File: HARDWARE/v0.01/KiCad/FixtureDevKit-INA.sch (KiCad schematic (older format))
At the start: 40 parts, among them J100 INA_43, J101 INA_43, J102 INA_41, J103 INA_43, J92 INA_40, J93 INA_40, J94 INA_42, J95 INA_42, J96 INA_40, J97 INA_42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

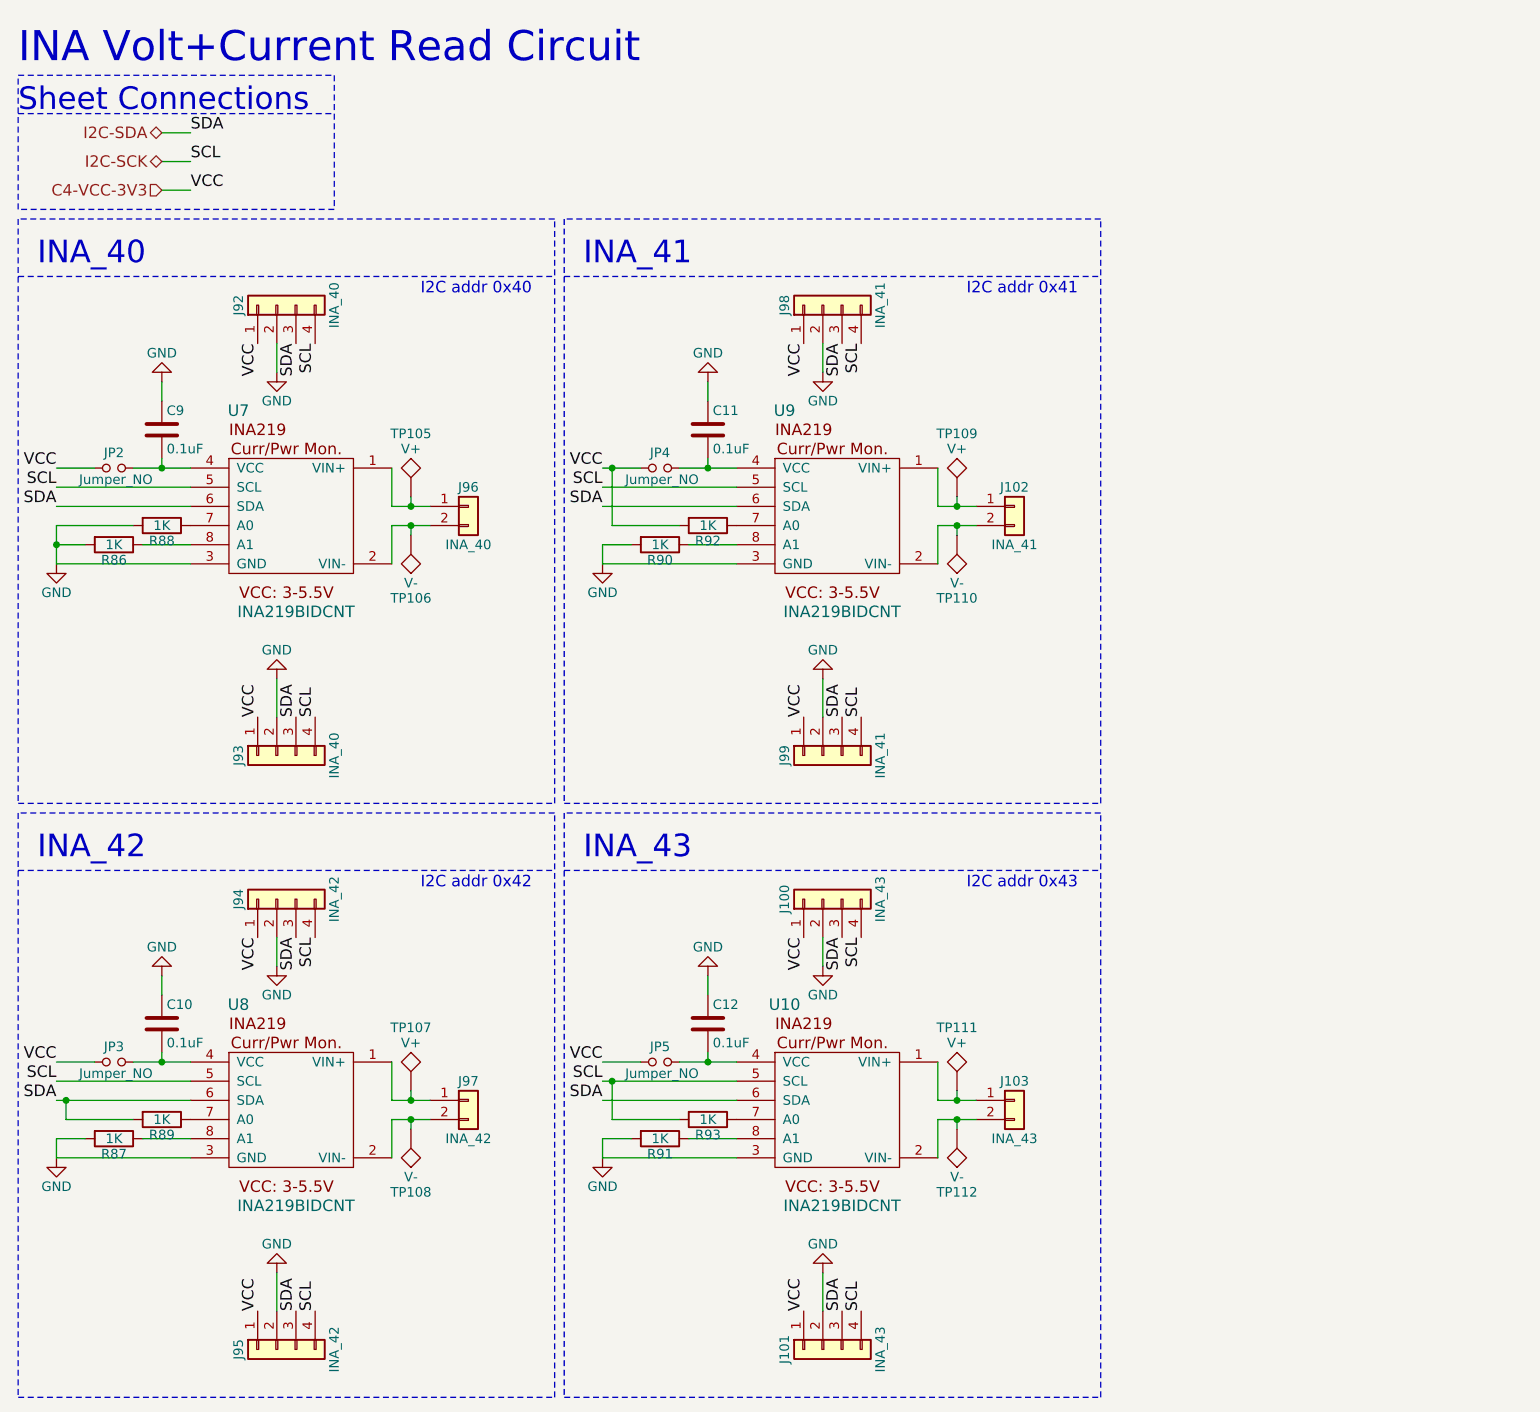
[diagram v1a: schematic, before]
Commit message: quasi-redoing entire schematic and layout
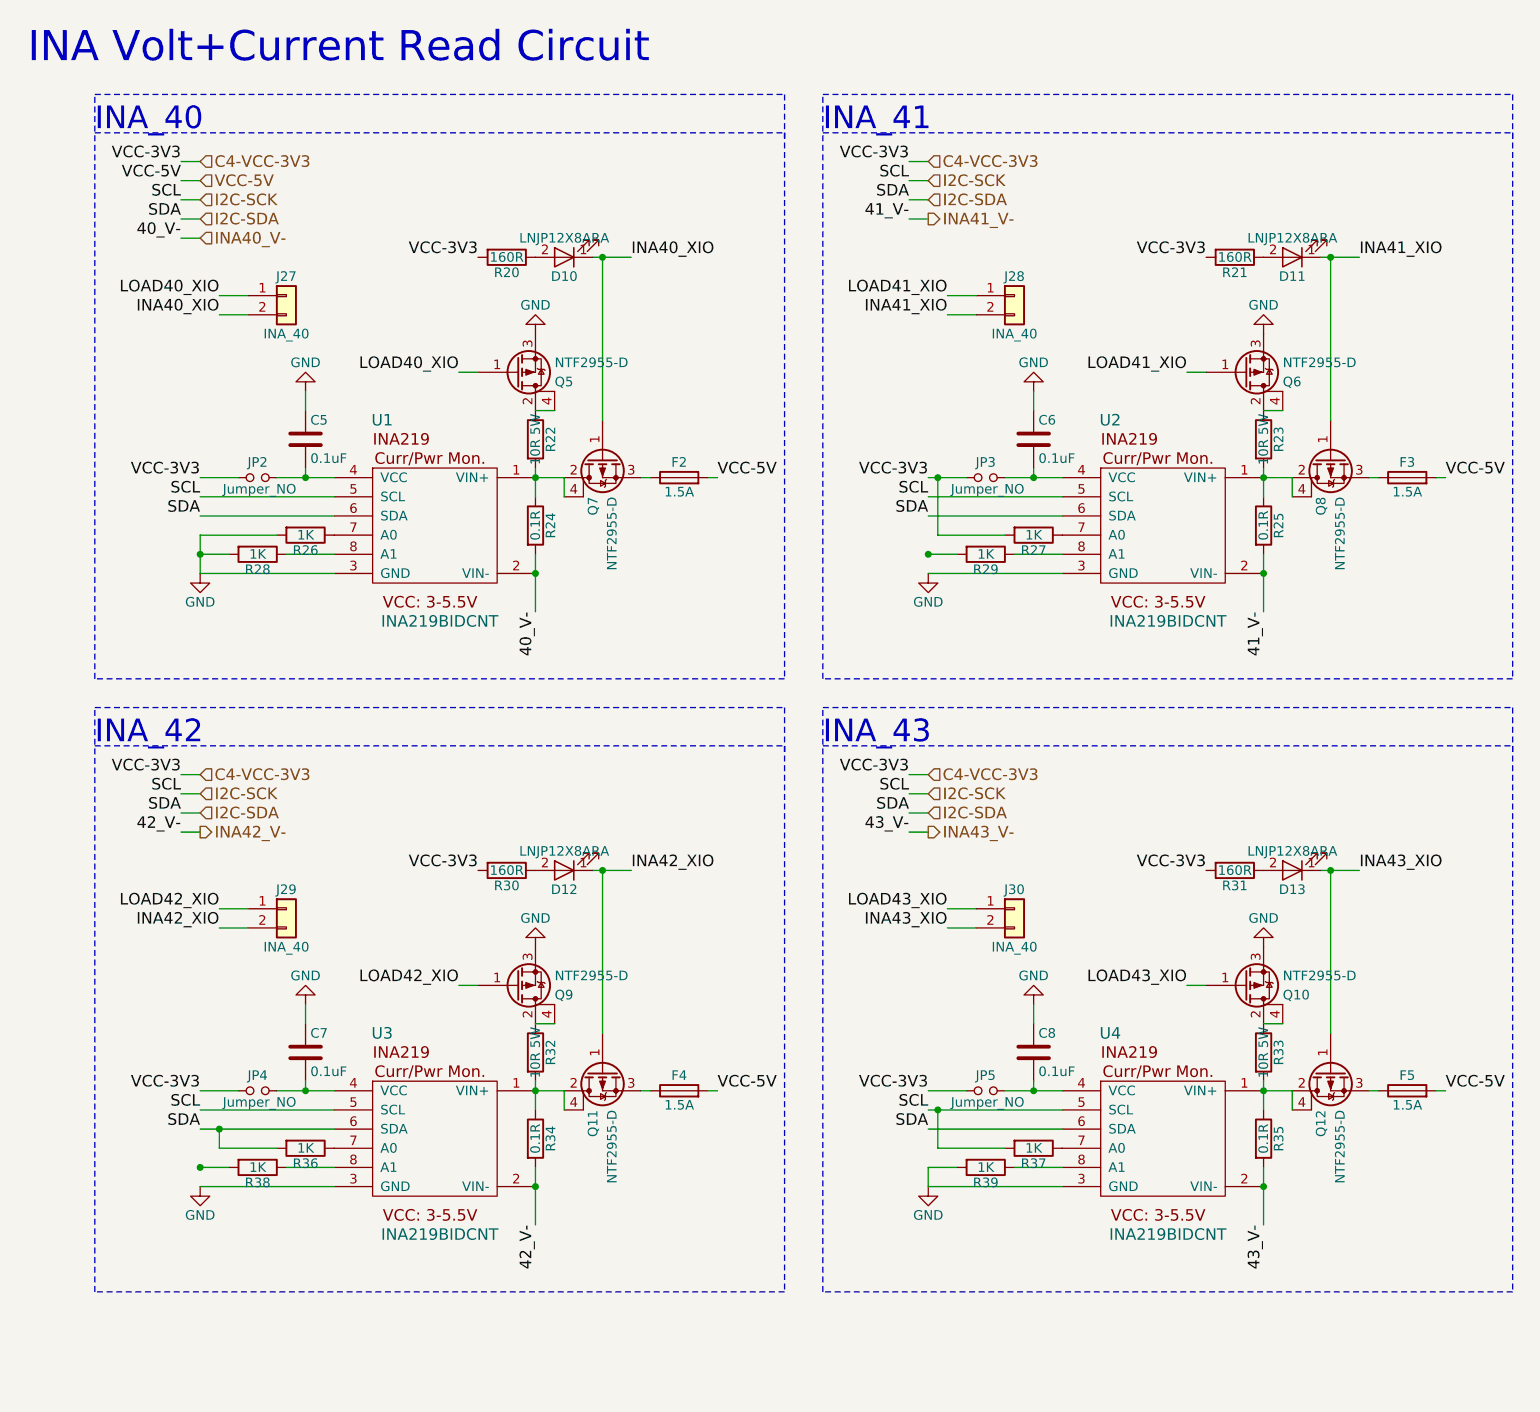
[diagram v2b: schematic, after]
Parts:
- removed C10, C11, C12: 0.1uF, Capacitors_SMD:C_0805_HandSoldering, symbol C
- removed J100, J101: INA_43, Pin_Headers:Pin_Header_Straight_1x04_Pitch2.54mm, symbol Conn_01x04
- removed J102: INA_41, Pin_Headers:Pin_Header_Straight_1x02_Pitch2.54mm, symbol Conn_01x02
- removed J103: INA_43, Pin_Headers:Pin_Header_Straight_1x02_Pitch2.54mm, symbol Conn_01x02
- removed J92, J93: INA_40, Pin_Headers:Pin_Header_Straight_1x04_Pitch2.54mm, symbol Conn_01x04
- removed J94, J95: INA_42, Pin_Headers:Pin_Header_Straight_1x04_Pitch2.54mm, symbol Conn_01x04
- removed J96: INA_40, Pin_Headers:Pin_Header_Straight_1x02_Pitch2.54mm, symbol Conn_01x02
- removed J97: INA_42, Pin_Headers:Pin_Header_Straight_1x02_Pitch2.54mm, symbol Conn_01x02
- removed J98, J99: INA_41, Pin_Headers:Pin_Header_Straight_1x04_Pitch2.54mm, symbol Conn_01x04
- removed R87, R89, R90, R91, R92, R93: 1K, Resistors_SMD:R_0805_HandSoldering, symbol R
- removed TP105, TP107, TP109, TP111: V+, TestPoint:TestPoint, symbol TEST
- removed TP106, TP108, TP110, TP112: V-, TestPoint:TestPoint, symbol TEST
- removed U10, U8, U9: INA219BIDCNT, INA219BIDCNR:SOT65P280X145-8N, symbol INA219BIDCNT
- added C6, C7, C8: 0.1uF, Capacitors_SMD:C_0805_HandSoldering, symbol C
- added D10, D11, D12, D13: LNJP12X8ARA, 1206:1206, symbol LED
- added F2, F3, F4, F5: 1.5A, 1206:1206, symbol Fuse
- added J27, J28, J29, J30: INA_40, Pin_Headers:Pin_Header_Straight_1x02_Pitch2.54mm, symbol Conn_01x02
- added Q10, Q11, Q12, Q5, Q6, Q7, Q8, Q9: NTF2955-D, NTF2955T1G:SOT230P700X180-4N, symbol Q_PMOS_GDSD
- added R20, R21, R30, R31: 160R, Resistors_SMD:R_0805_HandSoldering, symbol R
- added R22, R23, R32, R33: 10R 5W, RES_TWM3J560E:RES_TWM3J560E, symbol R
- added R24, R25, R34, R35: 0.1R, Resistors_SMD:R_0805_HandSoldering, symbol R
- added R27, R29, R36, R37, R38, R39: 1K, Resistors_SMD:R_0805_HandSoldering, symbol R
- added U2, U3, U4: INA219BIDCNT, INA219BIDCNR:SOT65P280X145-8N, symbol INA219BIDCNT
- renumbered C9 to C5, R88 to R26, R86 to R28, U7 to U1
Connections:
- net C4-VCC-3V3: now also R20.2, R21.2, R27.2, R30.2, R31.2
- net GND: now also C6.1, C7.1, C8.1, Q10.3 (S), Q5.3 (S), Q6.3 (S), Q9.3 (S), R39.2, U2.3 (GND), U3.3 (GND), U4.3 (GND)
- net I2C-SCK: now also R37.2, U2.5 (SCL), U3.5 (SCL), U4.5 (SCL)
- net I2C-SDA: now also R36.2, U2.6 (SDA), U3.6 (SDA), U4.6 (SDA)
- net at U1.1 (VIN+): now also Q7.2 (D), Q7.4 (D), R22.2, R24.1
- net INA40_V-: now reaches U1.2 (VIN-)
- net INA40_V-: now also R24.2
- net at JP4.2: now also C7.2, U3.4 (VCC)
- net at JP3.2: now also C6.2, U2.4 (VCC)
- net at JP5.2: now also C8.2, U4.4 (VCC)
- new net: F2.1, Q7.3 (S)
- new net: D10.2 (A), R20.1
- new net: Q5.2 (D), Q5.4 (D), R22.1
- new net: R27.1, U2.7 (A0)
- new net: R29.1, U2.8 (A1)
- new net: Q8.2 (D), Q8.4 (D), R23.2, R25.1, U2.1 (VIN+)
- new net: F3.1, Q8.3 (S)
- new net: D11.2 (A), R21.1
- new net: Q6.2 (D), Q6.4 (D), R23.1
- new net: R36.1, U3.7 (A0)
- new net: R38.1, U3.8 (A1)
- new net: Q11.2 (D), Q11.4 (D), R32.2, R34.1, U3.1 (VIN+)
- new net: F4.1, Q11.3 (S)
- new net: D12.2 (A), R30.1
- new net: Q9.2 (D), Q9.4 (D), R32.1
- new net: R37.1, U4.7 (A0)
- new net: R39.1, U4.8 (A1)
- new net: Q12.2 (D), Q12.4 (D), R33.2, R35.1, U4.1 (VIN+)
- new net: F5.1, Q12.3 (S)
- new net: D13.2 (A), R31.1
- new net: Q10.2 (D), Q10.4 (D), R33.1
- new net INA40_XIO: D10.1 (K), J27.2 (Pin_2), Q7.1 (G)
- new net INA41_V-: R25.2, U2.2 (VIN-)
- new net INA41_XIO: D11.1 (K), J28.2 (Pin_2), Q8.1 (G)
- new net INA42_V-: R34.2, U3.2 (VIN-)
- new net INA42_XIO: D12.1 (K), J29.2 (Pin_2), Q11.1 (G)
- new net INA43_V-: R35.2, U4.2 (VIN-)
- new net INA43_XIO: D13.1 (K), J30.2 (Pin_2), Q12.1 (G)
- new net LOAD40_XIO: J27.1 (Pin_1), Q5.1 (G)
- new net LOAD41_XIO: J28.1 (Pin_1), Q6.1 (G)
- new net LOAD42_XIO: J29.1 (Pin_1), Q9.1 (G)
- new net LOAD43_XIO: J30.1 (Pin_1), Q10.1 (G)
- new net VCC-5V: F2.2, F3.2, F4.2, F5.2
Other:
- note added: "INA_41"
- note removed: "I2C addr 0x40"
- note removed: "I2C addr 0x41\n"
- note removed: "I2C addr 0x42"
- note removed: "I2C addr 0x43"
- note removed: "INA_41\n"
- note removed: "Sheet Connections"
- moved on the sheet: C5, JP2, R26, R28, U1

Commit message: updating rough layout
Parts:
- added D18, D19, D20, D21: LNJP12X8ARA, 1206:1206, symbol LED
- added R17, R18, R56, R57: 160R, Resistors_SMD:R_0805_HandSoldering, symbol R
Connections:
- net C4-VCC-3V3: now also R17.2, R18.2, R56.2, R57.2
- net GND: now also R29.2, R38.2
- net LOAD40_XIO: now also D18.1 (K)
- net LOAD41_XIO: now also D19.1 (K)
- net LOAD42_XIO: now also D20.1 (K)
- net LOAD43_XIO: now also D21.1 (K)
- new net: D18.2 (A), R17.1
- new net: D19.2 (A), R18.1
- new net: D21.2 (A), R57.1
- new net: D20.2 (A), R56.1
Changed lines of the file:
@@
 $EndComp
 $Comp
-L GND #PWR034
+L GND #PWR029
 U 1 1 59F0363E
 P 2050 2450
-F 0 "#PWR034" H 2050 2200 50  0001 C CNN
+F 0 "#PWR029" H 2050 2200 50  0001 C CNN
 F 1 "GND" H 2050 2300 50  0000 C CNN
 F 2 "" H 2050 2450 50  0001 C CNN
@@
 	1500 3100 2200 3100
 $Comp
-L GND #PWR035
+L GND #PWR030
 U 1 1 59F06DD3
 P 1500 3400
-F 0 "#PWR035" H 1500 3150 50  0001 C CNN
+F 0 "#PWR030" H 1500 3150 50  0001 C CNN
 F 1 "GND" H 1500 3250 50  0000 C CNN
 F 2 "" H 1500 3400 50  0001 C CNN
@@
 Connection ~ 3250 2900
 $Comp
-L GND #PWR036
+L GND #PWR031
 U 1 1 59F80F3B
 P 3250 2150
-F 0 "#PWR036" H 3250 1900 50  0001 C CNN
+F 0 "#PWR031" H 3250 1900 50  0001 C CNN
 F 1 "GND" H 3250 2000 50  0000 C CNN
 F 2 "" H 3250 2150 50  0001 C CNN
@@
 $EndComp
 $Comp
-L GND #PWR037
+L GND #PWR032
 U 1 1 59FAD47F
 P 5850 2450
-F 0 "#PWR037" H 5850 2200 50  0001 C CNN
+F 0 "#PWR032" H 5850 2200 50  0001 C CNN
 F 1 "GND" H 5850 2300 50  0000 C CNN
 F 2 "" H 5850 2450 50  0001 C CNN
@@
 	5300 3100 6000 3100
 $Comp
-L GND #PWR038
+L GND #PWR033
 U 1 1 59FAD4A2
 P 5300 3400
-F 0 "#PWR038" H 5300 3150 50  0001 C CNN
+F 0 "#PWR033" H 5300 3150 50  0001 C CNN
 F 1 "GND" H 5300 3250 50  0000 C CNN
 F 2 "" H 5300 3400 50  0001 C CNN
@@
 Connection ~ 7050 2900
 $Comp
-L GND #PWR039
+L GND #PWR034
 U 1 1 59FAD4ED
 P 7050 2150
-F 0 "#PWR039" H 7050 1900 50  0001 C CNN
+F 0 "#PWR034" H 7050 1900 50  0001 C CNN
 F 1 "GND" H 7050 2000 50  0000 C CNN
 F 2 "" H 7050 2150 50  0001 C CNN
@@
 $EndComp
 $Comp
-L GND #PWR040
+L GND #PWR035
 U 1 1 59FAE04E
 P 2050 5650
-F 0 "#PWR040" H 2050 5400 50  0001 C CNN
+F 0 "#PWR035" H 2050 5400 50  0001 C CNN
 F 1 "GND" H 2050 5500 50  0000 C CNN
 F 2 "" H 2050 5650 50  0001 C CNN
@@
 	1500 6300 2200 6300
 $Comp
-L GND #PWR041
+L GND #PWR036
 U 1 1 59FAE071
 P 1500 6600
-F 0 "#PWR041" H 1500 6350 50  0001 C CNN
+F 0 "#PWR036" H 1500 6350 50  0001 C CNN
 F 1 "GND" H 1500 6450 50  0000 C CNN
 F 2 "" H 1500 6600 50  0001 C CNN
@@
 Connection ~ 3250 6100
 $Comp
-L GND #PWR042
+L GND #PWR037
 U 1 1 59FAE0BC
 P 3250 5350
-F 0 "#PWR042" H 3250 5100 50  0001 C CNN
+F 0 "#PWR037" H 3250 5100 50  0001 C CNN
 F 1 "GND" H 3250 5200 50  0000 C CNN
 F 2 "" H 3250 5350 50  0001 C CNN
@@
 $EndComp
 $Comp
-L GND #PWR043
+L GND #PWR038
 U 1 1 59FAE0E9
 P 5850 5650
-F 0 "#PWR043" H 5850 5400 50  0001 C CNN
+F 0 "#PWR038" H 5850 5400 50  0001 C CNN
 F 1 "GND" H 5850 5500 50  0000 C CNN
 F 2 "" H 5850 5650 50  0001 C CNN
@@
 	5300 6300 6000 6300
 $Comp
-L GND #PWR044
+L GND #PWR039
 U 1 1 59FAE10C
 P 5300 6600
-F 0 "#PWR044" H 5300 6350 50  0001 C CNN
+F 0 "#PWR039" H 5300 6350 50  0001 C CNN
 F 1 "GND" H 5300 6450 50  0000 C CNN
 F 2 "" H 5300 6600 50  0001 C CNN
@@
 Connection ~ 7050 6100
 $Comp
-L GND #PWR045
+L GND #PWR040
 U 1 1 59FAE157
 P 7050 5350
-F 0 "#PWR045" H 7050 5100 50  0001 C CNN
+F 0 "#PWR040" H 7050 5100 50  0001 C CNN
 F 1 "GND" H 7050 5200 50  0000 C CNN
 F 2 "" H 7050 5350 50  0001 C CNN
@@
 	5350 6400 5350 6200
 Connection ~ 5350 6200
+$Comp
+L LED D18
+U 1 1 59F8B565
+P 2700 2150
+F 0 "D18" H 2700 2250 50  0000 C CNN
+F 1 "LNJP12X8ARA" H 2700 2050 50  0000 C CNN
+F 2 "1206:1206" H 2700 2150 50  0001 C CNN
+F 3 "" H 2700 2150 50  0001 C CNN
+	1    2700 2150
+	-1   0    0    1
+$EndComp
+$Comp
+L R R17
+U 1 1 59F8B6D7
+P 2400 2150
+F 0 "R17" V 2480 2150 50  0000 C CNN
+F 1 "160R" V 2400 2150 50  0000 C CNN
+F 2 "Resistors_SMD:R_0805_HandSoldering" V 2330 2150 50  0001 C CNN
+F 3 "" H 2400 2150 50  0001 C CNN
+	1    2400 2150
+	0    1    1    0
+$EndComp
+Text Label 2250 2150 1    60   ~ 0
+VCC-3V3
+Wire Wire Line
+	2850 2350 2850 2150
+$Comp
+L LED D19
+U 1 1 59F8C237
+P 6500 2150
+F 0 "D19" H 6500 2250 50  0000 C CNN
+F 1 "LNJP12X8ARA" H 6500 2050 50  0000 C CNN
+F 2 "1206:1206" H 6500 2150 50  0001 C CNN
+F 3 "" H 6500 2150 50  0001 C CNN
+	1    6500 2150
+	-1   0    0    1
+$EndComp
+$Comp
+L R R18
+U 1 1 59F8C23D
+P 6200 2150
+F 0 "R18" V 6280 2150 50  0000 C CNN
+F 1 "160R" V 6200 2150 50  0000 C CNN
+F 2 "Resistors_SMD:R_0805_HandSoldering" V 6130 2150 50  0001 C CNN
+F 3 "" H 6200 2150 50  0001 C CNN
+	1    6200 2150
+	0    1    1    0
+$EndComp
+Text Label 6050 2150 1    60   ~ 0
+VCC-3V3
+Wire Wire Line
+	6650 2350 6650 2150
+$Comp
+L LED D21
+U 1 1 59F8C78D
+P 6500 5350
+F 0 "D21" H 6500 5450 50  0000 C CNN
+F 1 "LNJP12X8ARA" H 6500 5250 50  0000 C CNN
+F 2 "1206:1206" H 6500 5350 50  0001 C CNN
+F 3 "" H 6500 5350 50  0001 C CNN
+	1    6500 5350
+	-1   0    0    1
+$EndComp
+$Comp
+L R R57
+U 1 1 59F8C793
+P 6200 5350
+F 0 "R57" V 6280 5350 50  0000 C CNN
+F 1 "160R" V 6200 5350 50  0000 C CNN
+F 2 "Resistors_SMD:R_0805_HandSoldering" V 6130 5350 50  0001 C CNN
+F 3 "" H 6200 5350 50  0001 C CNN
+	1    6200 5350
+	0    1    1    0
+$EndComp
+Text Label 6050 5350 1    60   ~ 0
+VCC-3V3
+Wire Wire Line
+	6650 5550 6650 5350
+$Comp
+L LED D20
+U 1 1 59F8CBDA
+P 2700 5300
+F 0 "D20" H 2700 5400 50  0000 C CNN
+F 1 "LNJP12X8ARA" H 2700 5200 50  0000 C CNN
+F 2 "1206:1206" H 2700 5300 50  0001 C CNN
+F 3 "" H 2700 5300 50  0001 C CNN
+	1    2700 5300
+	-1   0    0    1
+$EndComp
+$Comp
+L R R56
+U 1 1 59F8CBE0
+P 2400 5300
+F 0 "R56" V 2480 5300 50  0000 C CNN
+F 1 "160R" V 2400 5300 50  0000 C CNN
+F 2 "Resistors_SMD:R_0805_HandSoldering" V 2330 5300 50  0001 C CNN
+F 3 "" H 2400 5300 50  0001 C CNN
+	1    2400 5300
+	0    1    1    0
+$EndComp
+Text Label 2250 5300 1    60   ~ 0
+VCC-3V3
+Wire Wire Line
+	2850 5550 2850 5300
+Wire Wire Line
+	5300 3300 5300 3400
+Wire Wire Line
+	1500 6500 1500 6600
 $EndSCHEMATC
